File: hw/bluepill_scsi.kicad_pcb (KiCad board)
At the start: 2 copper layers, 43.8 x 73.7 mm, 14 parts, among them J1 Micro_SD_Card, J2 Conn_02x25_Odd_Even, J3 Programming Pins, J4 Berg Power Connector, U1 BluePill_STM32F103C

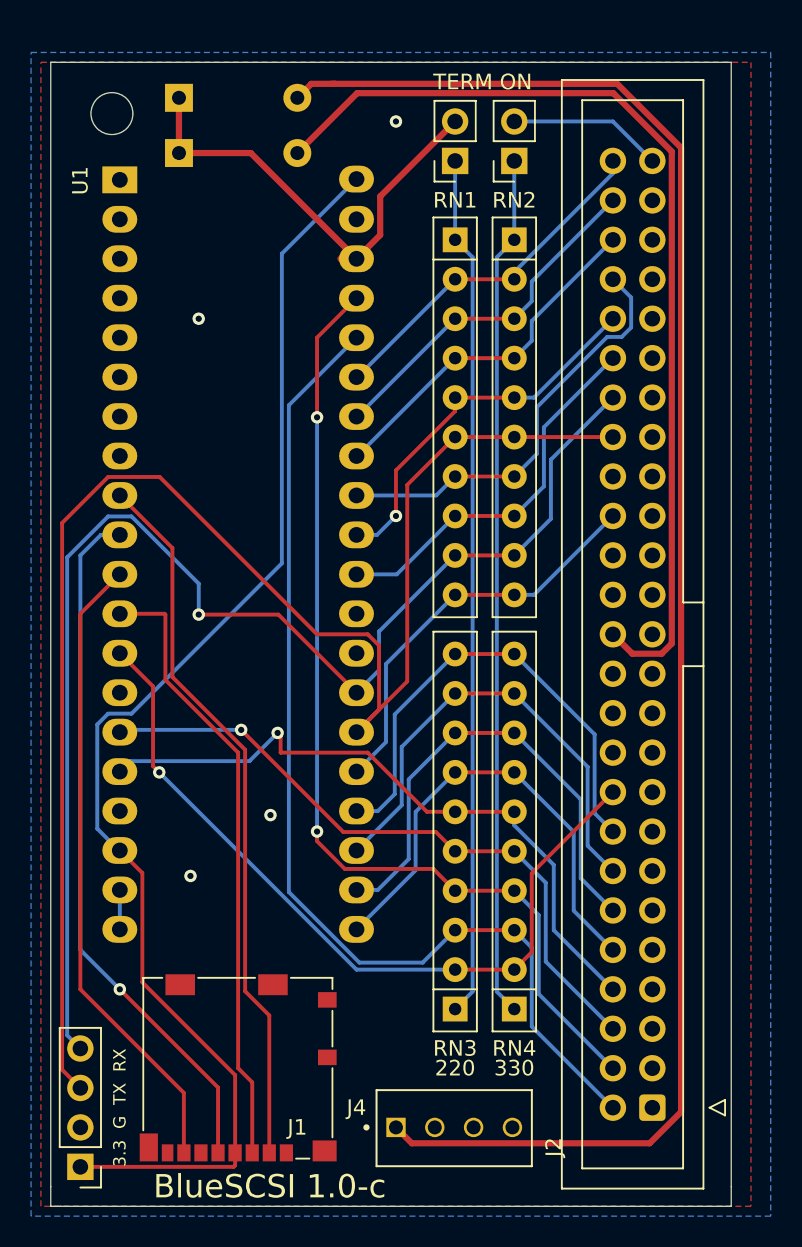
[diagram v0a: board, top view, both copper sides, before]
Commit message: Added rough cut of STM32
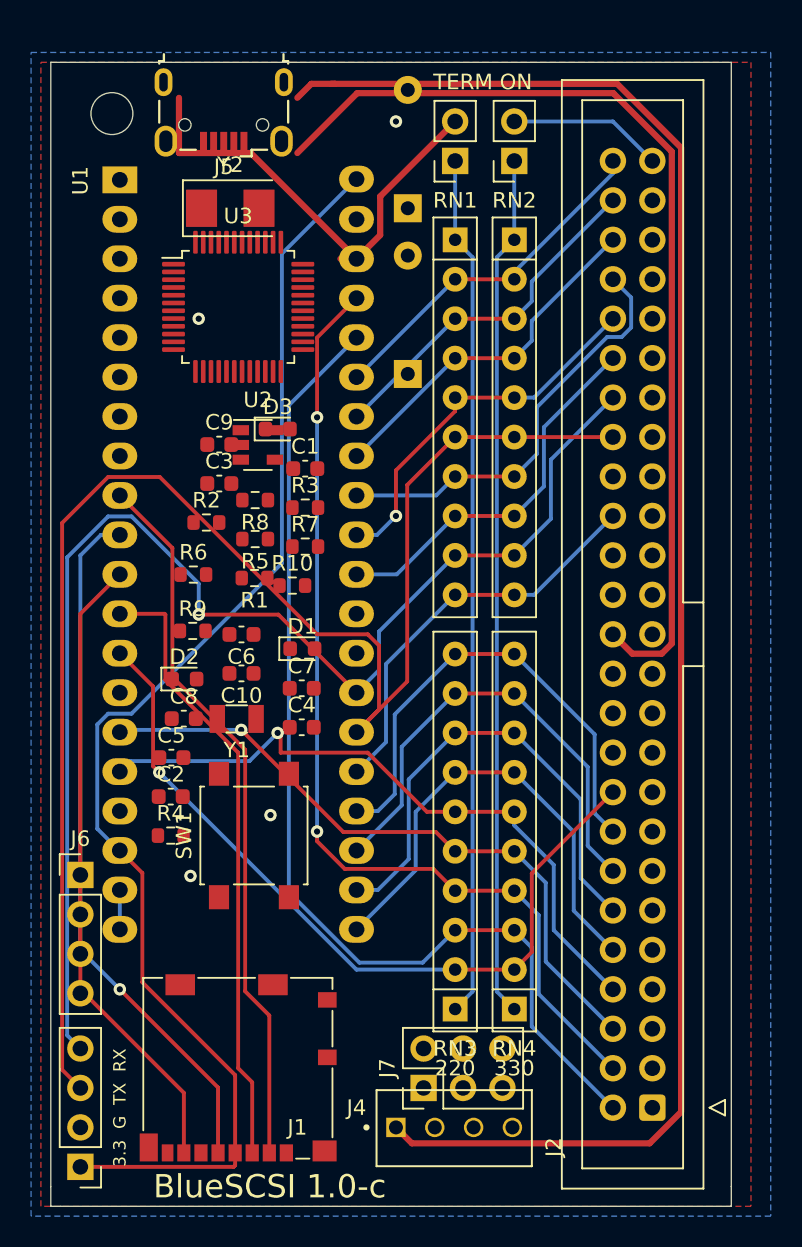
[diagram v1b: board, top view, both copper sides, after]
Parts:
- added C1: 20p, Capacitor_SMD:C_0603_1608Metric, F.Cu at (87.5, 101.7)
- added C10: 100nF, Capacitor_SMD:C_0603_1608Metric, F.Cu at (83.4, 114.9)
- added C2: 20p, Capacitor_SMD:C_0603_1608Metric, F.Cu at (78.8, 122.8)
- added C3: 100nF, Capacitor_SMD:C_0603_1608Metric, F.Cu at (82.0, 102.7)
- added C4: 20p, Capacitor_SMD:C_0603_1608Metric, F.Cu at (87.3, 118.4)
- added C5: 20p, Capacitor_SMD:C_0603_1608Metric, F.Cu at (78.9, 120.3)
- added C6: 100nF, Capacitor_SMD:C_0603_1608Metric, F.Cu at (83.4, 112.4)
- added C7: 100nF, Capacitor_SMD:C_0603_1608Metric, F.Cu at (87.3, 115.9)
- added C8: 100nF, Capacitor_SMD:C_0603_1608Metric, F.Cu at (79.7, 117.8)
- added C9: 100nF, Capacitor_SMD:C_0603_1608Metric, F.Cu at (82.0, 100.2)
- added D1: LED_Small, LED_SMD:LED_0603_1608Metric, F.Cu at (87.3, 113.3)
- added D2: LED_Small, LED_SMD:LED_0603_1608Metric, F.Cu at (79.7, 115.3)
- added D3: LED_Small, LED_SMD:LED_0603_1608Metric, F.Cu at (85.7, 99.2)
- added J5: USB_B_Micro, Connector_USB:USB_Micro-B_Wuerth_629105150521, F.Cu at (82.3, 78.8)
- added J6: Conn_01x04_Male, Connector_PinHeader_2.54mm:PinHeader_1x04_P2.54mm_Vertical, F.Cu at (73.0, 127.9)
- added J7: Conn_02x03_Odd_Even, Connector_PinHeader_2.54mm:PinHeader_2x03_P2.54mm_Vertical, F.Cu at (95.1, 141.6)
- added R1: 100k, Resistor_SMD:R_0603_1608Metric, F.Cu at (84.2, 108.8)
- added R10: 100k, Resistor_SMD:R_0603_1608Metric, F.Cu at (86.7, 109.3)
- added R2: 4.7k, Resistor_SMD:R_0603_1608Metric, F.Cu at (81.1, 105.2)
- added R3: 4.7k, Resistor_SMD:R_0603_1608Metric, F.Cu at (87.5, 104.2)
- added R4: 20, Resistor_SMD:R_0603_1608Metric, F.Cu at (78.8, 125.4)
- added R5: 20, Resistor_SMD:R_0603_1608Metric, F.Cu at (84.3, 106.3)
- added R6: 4.7k, Resistor_SMD:R_0603_1608Metric, F.Cu at (80.3, 108.5)
- added R7: 1M, Resistor_SMD:R_0603_1608Metric, F.Cu at (87.5, 106.7)
- added R8: 4.7k, Resistor_SMD:R_0603_1608Metric, F.Cu at (84.3, 103.8)
- added R9: 100k, Resistor_SMD:R_0603_1608Metric, F.Cu at (80.3, 112.2)
- added SW1: SW_Push, Button_Switch_SMD:SW_SPST_B3S-1000, F.Cu at (84.2, 125.3)
- added U2: MIC5504-3.3YM5, Package_TO_SOT_SMD:SOT-23-5, F.Cu at (84.5, 100.2)
- added U3: STM32F103C8Tx, Package_QFP:LQFP-48_7x7mm_P0.5mm, F.Cu at (83.2, 91.3)
- added Y1: 32.768k, Crystal:Crystal_SMD_3215-2Pin_3.2x1.5mm, F.Cu at (83.1, 117.8)
- added Y2: 8MHz, Crystal:Crystal_SMD_5032-2Pin_5.0x3.2mm, F.Cu at (82.7, 85.0)
- moved D5 20.5 mm to (94.1, 95.6), turned to 90 degrees
- moved D4 16.4 mm to (94.1, 85.0), turned to 90 degrees
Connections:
- net /SCSI_ACK renamed SCSI_ACK
- net /SCSI_ATN renamed SCSI_ATN
- net /SCSI_BSY renamed SCSI_BSY
- net /SCSI_CD renamed SCSI_CD
- net /SCSI_DAT0 renamed SCSI_DAT0
- net /SCSI_DAT1 renamed SCSI_DAT1
- net /SCSI_DAT2 renamed SCSI_DAT2
- net /SCSI_DAT3 renamed SCSI_DAT3
- net /SCSI_DAT4 renamed SCSI_DAT4
- net /SCSI_DAT5 renamed SCSI_DAT5
- net /SCSI_DAT6 renamed SCSI_DAT6
- net /SCSI_DAT7 renamed SCSI_DAT7
- net /SCSI_DBP renamed SCSI_DATP
- net /SCSI_IO renamed SCSI_IO
- net /SCSI_MSG renamed SCSI_MSG
- net /SCSI_REQ renamed SCSI_REQ
- net /SCSI_RST renamed SCSI_RST
- net /SCSI_SEL renamed SCSI_SEL
- net /SD_CLK renamed SD_CLK
- net /SD_CS renamed SD_CS
- J1 pad 3: /SD_MOSI -> SD_MISO
- J1 pad 7: /SD_MISO -> SD_MISO
- U1 pad 11: /SD_MISO -> SD_MISO
- U1 pad 12: /SD_MOSI -> SD_MISO
- U1 pad 2: /LED -> DBG_LED
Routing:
- net SD_MISO: track 0.00 -> 81.0 mm
- net /SD_MISO: track 41.1 -> 0.00 mm
- net /SD_MOSI: track 39.9 -> 0.00 mm

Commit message: Updated bluepill all-in-one
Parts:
- removed the C2 at (78.8, 122.8)
- removed the J1 at (83.2, 140.3)
- removed the R10 at (86.7, 109.3)
- added C12: 20p, Capacitor_SMD:C_0603_1608Metric, F.Cu at (80.1, 102.7)
- added C5: 1uF, Capacitor_SMD:C_0603_1608Metric, F.Cu at (86.7, 90.3)
- added C6: 1uF, Capacitor_SMD:C_0603_1608Metric, F.Cu at (87.2, 87.8)
- added C7: 1uF, Capacitor_SMD:C_0603_1608Metric, F.Cu at (87.2, 86.2)
- added J6: Micro_SD_Card, Connector_Card:microSD_HC_Molex_104031-0811, F.Cu at (83.2, 140.3)
- added J8: Conn_01x04_Male, Connector_PinHeader_2.54mm:PinHeader_1x04_P2.54mm_Vertical, F.Cu at (72.8, 83.2)
- added R4: 100k, Resistor_SMD:R_0603_1608Metric, F.Cu at (81.9, 123.6)
- D3: renamed from D4; moved to F.Cu
- D4: renamed from D5; moved to F.Cu
- R2: renamed from R1; value 100k -> 10k
- SW1: footprint Button_Switch_SMD:SW_SPST_B3S-1000 -> Button_Switch_SMD:SW_SPST_B3U-1000P
- moved R9 41.0 mm to (81.9, 84.5), turned to 90 degrees
- moved J2 37.4 mm to (87.2, 93.3), turned to 270 degrees
- moved U2 24.6 mm to (83.2, 116.0), turned to 315 degrees
- moved C2 23.6 mm to (84.5, 126.1), turned to 270 degrees
- moved Y2 22.6 mm to (83.7, 107.6)
- moved J7 22.3 mm to (79.1, 126.1), turned to 0 degrees
- moved R11 21.8 mm to (83.4, 84.5), turned to 270 degrees
- moved R10 19.3 mm to (85.0, 84.5), turned to 270 degrees
- moved D5 17.6 mm to (79.9, 97.7)
- moved D1 15.7 mm to (86.5, 97.7)
- moved C14 15.6 mm to (87.8, 107.6), turned to 90 degrees
- moved Y3 15.4 mm to (83.7, 102.5), turned to 0 degrees
- moved R2 15.2 mm to (87.5, 123.6), turned to 0 degrees
- moved C1 14.3 mm to (84.5, 129.2), turned to 270 degrees
- moved C13 13.2 mm to (79.6, 107.6), turned to 90 degrees
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- renumbered C10 to C1, C6 to C10, C7 to C11, C4 to C13, C5 to C14, C3 to C2, C8 to C3, C9 to C4, C1 to C9, D3 to D2, D2 to D5, J3 to J1, J6 to J2, J5 to J3, J2 to J5, R2 to R1, R8 to R10, R5 to R11, R9 to R3, R6 to R5, R7 to R6, R3 to R7, R4 to R9, U2 to U1, U3 to U2, U1 to U3, Y1 to Y3
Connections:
- net /Blue_Pill_Clone/BOOT_0 renamed /Onboard Blue Pil/BOOT_0
- net /Blue_Pill_Clone/OSCIN renamed /Onboard Blue Pil/OSCIN
- net /Blue_Pill_Clone/OSCOUT renamed /Onboard Blue Pil/OSCOUT
- net /Blue_Pill_Clone/PC14 renamed /Onboard Blue Pil/PC14
- net /Blue_Pill_Clone/PC15 renamed /Onboard Blue Pil/PC15
- net /Blue_Pill_Clone/Reset renamed /Onboard Blue Pil/Reset
- net /Blue_Pill_Clone/SWCLK renamed /Onboard Blue Pil/SWCLK
- net /Blue_Pill_Clone/SWDIO renamed /Onboard Blue Pil/SWDIO
- net /Blue_Pill_Clone/USB_Data_+ renamed /Onboard Blue Pil/USB_Data_+
- net /Blue_Pill_Clone/USB_Data_- renamed /Onboard Blue Pil/USB_Data_-
- C9 pad 2: Net-(C1-Pad2) -> GND
- D1 pad 1: GND -> Net-(D1-Pad1)
- D1 pad 2: Net-(D1-Pad2) -> +3V3
- D2 pad 1: DBG_LED -> Net-(D2-Pad1)
- D2 pad 2: Net-(D3-Pad2) -> +3V3
- D5 pad 1: GND -> Net-(D5-Pad1)
- D5 pad 2: Net-(D2-Pad2) -> +5V
- H1 pad 1: Net-(H1-Pad1) -> (no net)
- J3 pad 1: VBUS -> +5V
- J3 pad 4: Net-(J5-Pad4) -> (no net)
- J4 pad 3: Net-(J4-Pad3) -> (no net)
- J4 pad 4: Net-(J4-Pad4) -> (no net)
- J5 pad 25: Net-(J2-Pad25) -> (no net)
- J5 pad 34: Net-(J2-Pad34) -> (no net)
- R1 pad 1: Net-(D1-Pad2) -> GND
- R1 pad 2: +3V3 -> Net-(D1-Pad1)
- R10 pad 1: VBUS -> +5V
- R5 pad 1: Net-(D3-Pad2) -> DBG_LED
- R5 pad 2: +3V3 -> Net-(D2-Pad1)
- R7 pad 1: Net-(D2-Pad2) -> GND
- R7 pad 2: +5V -> Net-(D5-Pad1)
- U1 pad 3: +5V -> (no net)
- U1 pad 4: Net-(U2-Pad4) -> (no net)
- U2 pad 1: Net-(U3-Pad1) -> (no net)
- U2 pad 10: Net-(U3-Pad10) -> (no net)
- U2 pad 11: Net-(U3-Pad11) -> (no net)
- U2 pad 12: Net-(U3-Pad12) -> USART2_RxD
- U2 pad 13: Net-(U3-Pad13) -> USART2_TxD
- U2 pad 19: Net-(U3-Pad19) -> (no net)
- U2 pad 20: /Blue_Pill_Clone/BOOT_1 -> /Onboard Blue Pil/BOOT_1
- U3 pad 1: Net-(U1-Pad1) -> (no net)
- U3 pad 14: Net-(U1-Pad14) -> (no net)
- U3 pad 17: Net-(U1-Pad17) -> (no net)
- U3 pad 28: Net-(U1-Pad28) -> (no net)
- U3 pad 29: Net-(U1-Pad29) -> (no net)
- U3 pad 3: Net-(U1-Pad3) -> (no net)
- U3 pad 4: Net-(U1-Pad4) -> (no net)
- U3 pad 5: Net-(U1-Pad5) -> (no net)
- U3 pad 6: Net-(U1-Pad6) -> (no net)
- U3 pad 7: Net-(U1-Pad7) -> (no net)
- U3 pad 8: Net-(U1-Pad8) -> (no net)
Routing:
- net GND: track 12.5 -> 191.4 mm, vias 4 -> 27
- net +3V3: track 85.0 -> 164.0 mm, vias 0 -> 13
- net SD_CS: track 46.3 -> 86.9 mm, vias 0 -> 7
- net /Onboard Blue Pil/USB_Data_-: track 0.00 -> 38.4 mm, vias 0 -> 2
- net /Onboard Blue Pil/USB_Data_+: track 0.00 -> 37.7 mm, vias 0 -> 2
- net DBG_LED: track 0.00 -> 36.5 mm, vias 0 -> 3
- net USART2_RxD: track 0.00 -> 36.1 mm, vias 0 -> 2
- net USART2_TxD: track 0.00 -> 34.0 mm, vias 0 -> 2
- net SCSI_IO: track 23.0 -> 55.6 mm, vias 0 -> 5
- net SCSI_DAT1: track 64.1 -> 95.3 mm, vias 2 -> 4
- net /Onboard Blue Pil/SWDIO: track 0.00 -> 30.5 mm, vias 0 -> 1
- net /Onboard Blue Pil/SWCLK: track 0.00 -> 29.8 mm, vias 0 -> 1
- net SCSI_REQ: track 23.4 -> 51.7 mm, vias 0 -> 3
- net SCSI_DAT0: track 68.8 -> 95.2 mm, vias 0 -> 3
- net SCSI_DAT7: track 31.4 -> 54.4 mm, vias 0 -> 4
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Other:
- board text added: "BlueSCSI AIO Beta 1"
- board text removed: "BlueSCSI 1.0-c"

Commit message: As-ordered version
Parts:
- removed J1: Programming Pins, Connector_PinHeader_2.54mm:PinHeader_1x04_P2.54mm_Vertical
- removed RN1, RN3: 220, Resistor_THT:R_Array_SIP10
- removed RN2, RN4: 330, Resistor_THT:R_Array_SIP10
- added C15: 330, Resistor_SMD:R_0603_1608Metric, F.Cu at (102.0, 83.2)
- added C16: 220, Resistor_SMD:R_0603_1608Metric, F.Cu at (98.9, 85.5)
- added C17: 330, Resistor_SMD:R_0603_1608Metric, F.Cu at (102.0, 85.5)
- added C18: 220, Resistor_SMD:R_0603_1608Metric, F.Cu at (98.9, 87.9)
- added C19: 330, Resistor_SMD:R_0603_1608Metric, F.Cu at (102.0, 87.9)
- added C20: 220, Resistor_SMD:R_0603_1608Metric, F.Cu at (98.9, 92.6)
- added C21: 330, Resistor_SMD:R_0603_1608Metric, F.Cu at (102.0, 92.6)
- added C22: 220, Resistor_SMD:R_0603_1608Metric, F.Cu at (98.9, 99.7)
- added C23: 330, Resistor_SMD:R_0603_1608Metric, F.Cu at (102.0, 99.7)
- added C24: 220, Resistor_SMD:R_0603_1608Metric, F.Cu at (98.9, 90.3)
- added C25: 330, Resistor_SMD:R_0603_1608Metric, F.Cu at (102.0, 90.3)
- added C26: 220, Resistor_SMD:R_0603_1608Metric, F.Cu at (98.9, 95.0)
- added C27: 330, Resistor_SMD:R_0603_1608Metric, F.Cu at (102.0, 95.0)
- added C28: 220, Resistor_SMD:R_0603_1608Metric, F.Cu at (98.9, 97.3)
- added C29: 330, Resistor_SMD:R_0603_1608Metric, F.Cu at (102.0, 97.3)
- added C30: 220, Resistor_SMD:R_0603_1608Metric, F.Cu at (98.9, 104.8)
- added C31: 330, Resistor_SMD:R_0603_1608Metric, F.Cu at (102.0, 104.8)
- added C32: 220, Resistor_SMD:R_0603_1608Metric, F.Cu at (98.9, 122.6)
- added C33: 330, Resistor_SMD:R_0603_1608Metric, F.Cu at (102.0, 122.6)
- added C34: 220, Resistor_SMD:R_0603_1608Metric, F.Cu at (98.9, 140.6)
- added C35: 330, Resistor_SMD:R_0603_1608Metric, F.Cu at (102.0, 140.6)
- added C36: 220, Resistor_SMD:R_0603_1608Metric, F.Cu at (98.9, 138.3)
- added C37: 330, Resistor_SMD:R_0603_1608Metric, F.Cu at (102.0, 138.3)
- added C38: 220, Resistor_SMD:R_0603_1608Metric, F.Cu at (98.9, 136.1)
- added C39: 330, Resistor_SMD:R_0603_1608Metric, F.Cu at (102.0, 136.1)
- added C40: 220, Resistor_SMD:R_0603_1608Metric, F.Cu at (98.9, 133.8)
- added C41: 330, Resistor_SMD:R_0603_1608Metric, F.Cu at (102.0, 133.8)
- added C42: 220, Resistor_SMD:R_0603_1608Metric, F.Cu at (98.9, 131.6)
- added C43: 330, Resistor_SMD:R_0603_1608Metric, F.Cu at (102.0, 131.6)
- added C44: 220, Resistor_SMD:R_0603_1608Metric, F.Cu at (98.9, 129.3)
- added C45: 330, Resistor_SMD:R_0603_1608Metric, F.Cu at (102.0, 129.3)
- added C46: 220, Resistor_SMD:R_0603_1608Metric, F.Cu at (98.9, 127.1)
- added C47: 330, Resistor_SMD:R_0603_1608Metric, F.Cu at (102.0, 127.1)
- added C48: 220, Resistor_SMD:R_0603_1608Metric, F.Cu at (98.9, 124.8)
- added C49: 330, Resistor_SMD:R_0603_1608Metric, F.Cu at (102.0, 124.8)
- added C8: 220, Resistor_SMD:R_0603_1608Metric, F.Cu at (98.9, 83.2)
- added D6: SM4007PL, Diode_SMD:D_SOD-123F, F.Cu at (92.5, 77.3)
- added D7: LED_Small, LED_SMD:LED_0603_1608Metric, F.Cu at (91.1, 145.4)
- added F1: 1A, Fuse:Fuse_1206_3216Metric, F.Cu at (93.9, 86.7)
- added R8: 4.7k, Resistor_SMD:R_0603_1608Metric, F.Cu at (91.1, 142.4)
- added TP1: TestPoint_Small, TestPoint:TestPoint_Pad_D1.5mm, B.Cu at (83.2, 77.3)
- added TP2: TestPoint_Small, TestPoint:TestPoint_Pad_D1.5mm, F.Cu at (79.1, 89.0)
- added TP3: TestPoint_Small, TestPoint:TestPoint_Pad_D1.5mm, F.Cu at (79.1, 86.0)
- added TP4: TestPoint_Small, TestPoint:TestPoint_Pad_D1.5mm, F.Cu at (72.8, 94.6)
- added TP5: TestPoint_Small, TestPoint:TestPoint_Pad_D1.5mm, F.Cu at (72.8, 91.1)
- added TP6: TestPoint_Small, TestPoint:TestPoint_Pad_D1.5mm, B.Cu at (88.5, 144.9)
- D3, D4: value Diode -> SM4007PL; footprint Diode_THT:D_A-405_P7.62mm_Horizontal -> Diode_SMD:D_SOD-123F
- R10: value 4.7k -> 1.5
- moved J8 63.2 mm to (73.3, 146.4), turned to 180 degrees
- moved D3 52.7 mm to (93.3, 137.7), turned to 270 degrees
- moved D4 15.8 mm to (92.5, 79.9), turned to 180 degrees
- moved JP1 1.27 mm to (101.0, 80.6)
- moved JP2 1.27 mm to (97.2, 80.6)
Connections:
- C5 pad 1: +5V -> VCC
- D3 pad 1: VCC -> +5V
- D3 pad 2: +5V -> /BERG_5V
- D4 pad 1: VCC -> +5V
- D5 pad 2: +5V -> VCC
- J3 pad 1: +5V -> VBUS
- J3 pad 4: (no net) -> Net-(J3-Pad4)
- J4 pad 1: +5V -> /BERG_5V
- R10 pad 1: +5V -> +3V3
- U1 pad 1: +5V -> VCC
- U1 pad 3: (no net) -> VCC
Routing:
- net GND: track 191.4 -> 288.8 mm, vias 27 -> 39
- net SCSI_BSY: track 85.2 -> 42.4 mm, vias 5 -> 4
- net SCSI_ACK: track 99.9 -> 62.4 mm, vias 6 -> 5
- net Net-(C16-Pad1): track 55.5 -> 86.2 mm, vias 0 -> 18
- net Net-(C15-Pad1): track 55.5 -> 84.7 mm, vias 0 -> 18
- net +5V: track 108.4 -> 80.0 mm
- net VCC: track 25.5 -> 48.1 mm, vias 2 -> 5
- net SCSI_DATP: track 66.4 -> 50.8 mm, vias 3 -> 6
- net SCSI_DAT7: track 54.4 -> 38.9 mm
- net SCSI_DAT1: track 95.3 -> 105.9 mm
- net SCSI_DAT0: track 95.2 -> 105.3 mm, vias 3 -> 5
- net /TERM_PWR: track 44.4 -> 53.8 mm
- net VBUS: track 0.00 -> 8.12 mm
- net SCSI_DAT6: track 50.0 -> 42.9 mm
- net Net-(J3-Pad4): track 0.00 -> 7.07 mm, vias 0 -> 1
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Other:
- rule pad_to_mask_clearance: 0.05 -> 0
- board text added: "+5V"
- board text added: "3.3 RX TX Gnd"
- board text added: "3.3v"
- board text added: "3v3"
- board text added: "5v"
- board text added: "ACK"
- board text added: "ATN"
- board text added: "BAD WOLF"
- board text added: "BOOT0"
- board text added: "BOOT1"
- board text added: "BSY"
- board text added: "BlueSCSI AIO Beta 2"
- board text added: "CD"
- board text added: "CLK"
- board text added: "D0"
- board text added: "D1"
- board text added: "D2"
- board text added: "D3"
- board text added: "D4"
- board text added: "D5"
- board text added: "D6"
- board text added: "D7"
- board text added: "DBG"
- board text added: "DIO"
- board text added: "DP"
- board text added: "GND"
- board text added: "IO"
- board text added: "MSG"
- board text added: "PC13"
- board text added: "REQ"
- board text added: "RESET"
- board text added: "RST"
- board text added: "RX"
- board text added: "SEL"
- board text added: "TX"
- board text added: "USART2"
- board text added: "USB+"
- board text added: "USB-"
- board text added: "VCC"
- board text removed: "3.3 G TX RX"
- board text removed: "BlueSCSI AIO Beta 1"
